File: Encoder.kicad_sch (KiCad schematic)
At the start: 13 parts, among them U5 AS5047D

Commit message: Add mcu connections
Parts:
- TP1, TP2, TP3, TP4, TP5, TP6: footprint (none) -> TestPoint:TestPoint_Pad_D1.0mm
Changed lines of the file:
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@@
 			)
 		)
-		(property "Footprint" ""
+		(property "Footprint" "TestPoint:TestPoint_Pad_D1.0mm"
 			(at 186.69 93.98 0)
 			(effects
@@
 			)
 		)
-		(property "Footprint" ""
+		(property "Footprint" "TestPoint:TestPoint_Pad_D1.0mm"
 			(at 173.99 85.09 0)
 			(effects
@@
 			)
 		)
-		(property "Footprint" ""
+		(property "Footprint" "TestPoint:TestPoint_Pad_D1.0mm"
 			(at 158.75 85.09 0)
 			(effects
@@
 			)
 		)
-		(property "Footprint" ""
+		(property "Footprint" "TestPoint:TestPoint_Pad_D1.0mm"
 			(at 166.37 85.09 0)
 			(effects
@@
 			)
 		)
-		(property "Footprint" ""
+		(property "Footprint" "TestPoint:TestPoint_Pad_D1.0mm"
 			(at 179.07 93.98 0)
 			(effects
@@
 			)
 		)
-		(property "Footprint" ""
+		(property "Footprint" "TestPoint:TestPoint_Pad_D1.0mm"
 			(at 194.31 93.98 0)
 			(effects

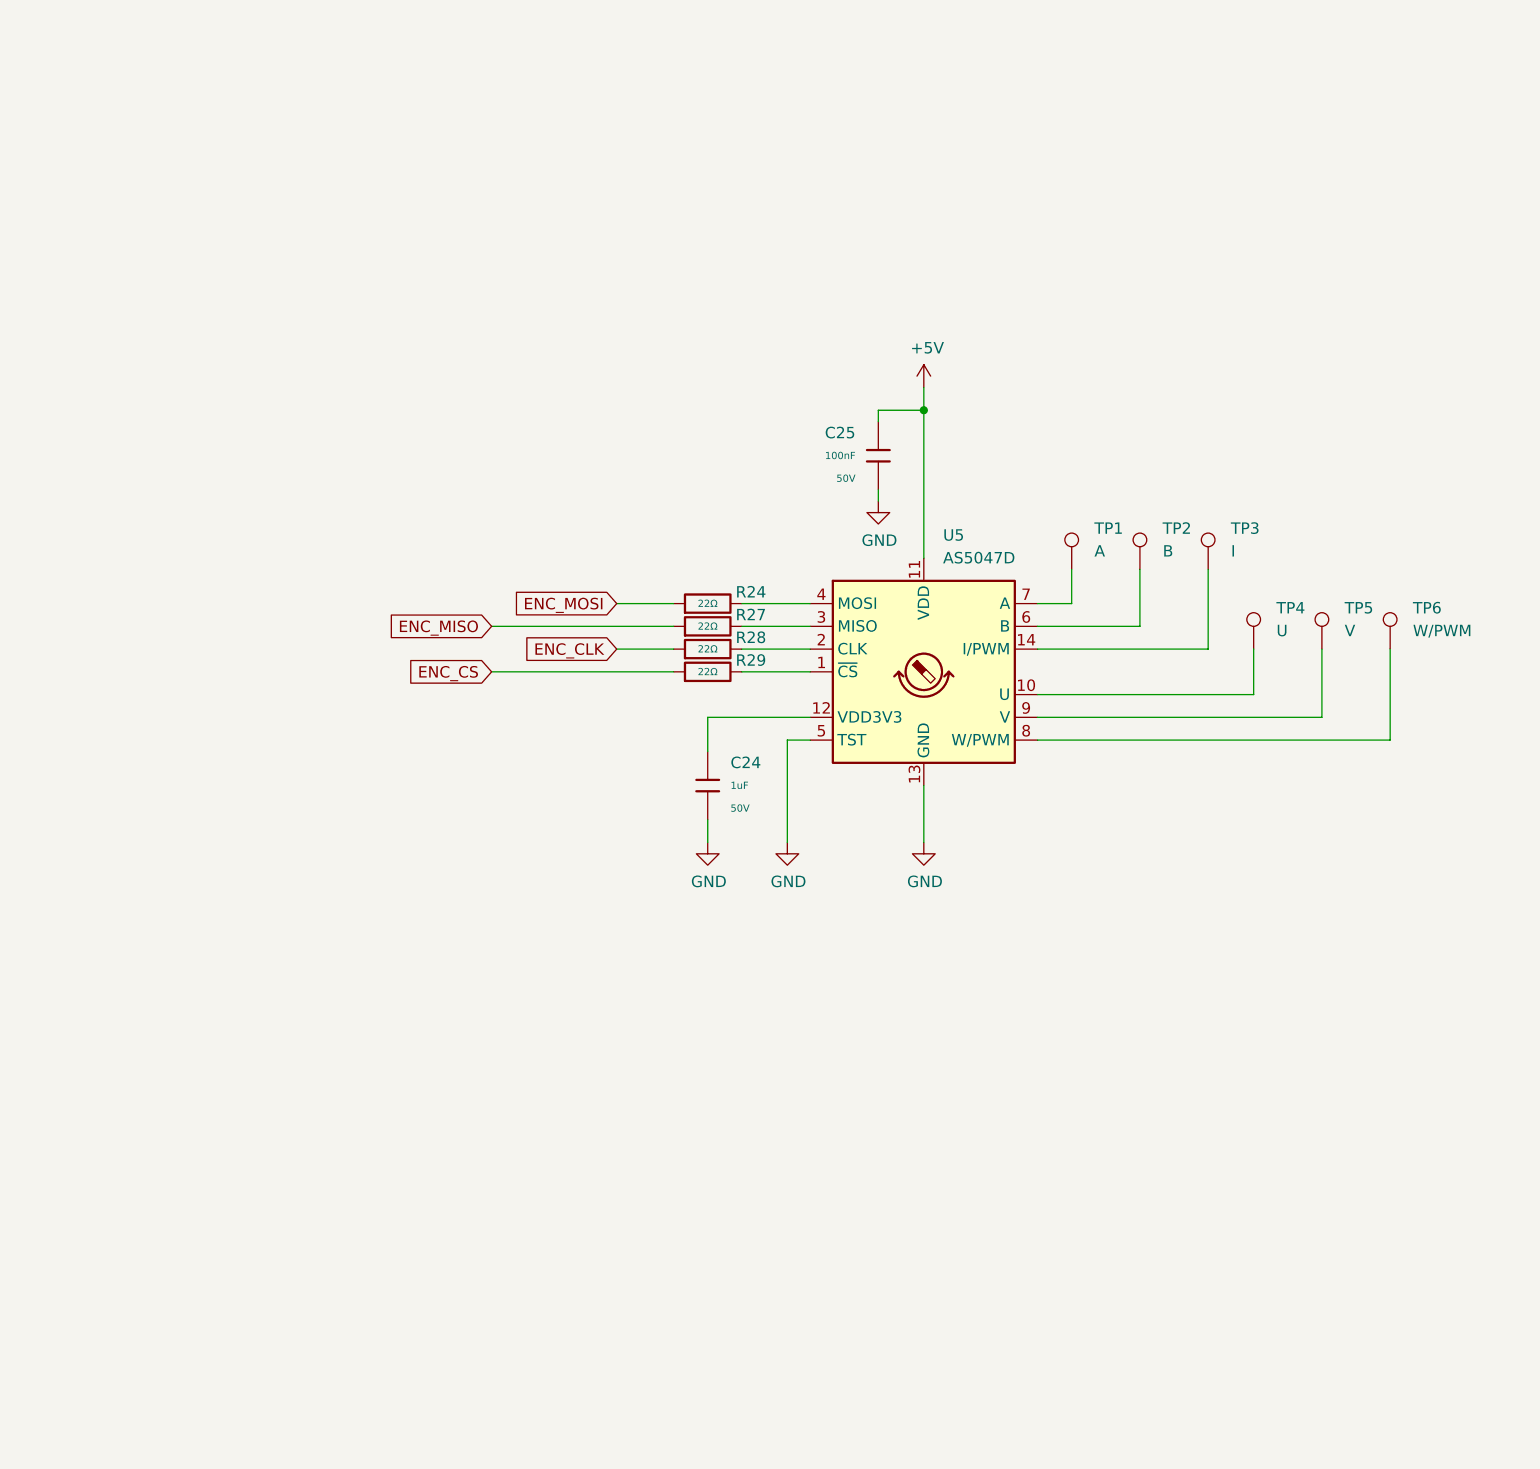
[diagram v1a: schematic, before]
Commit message: Added DRV layout
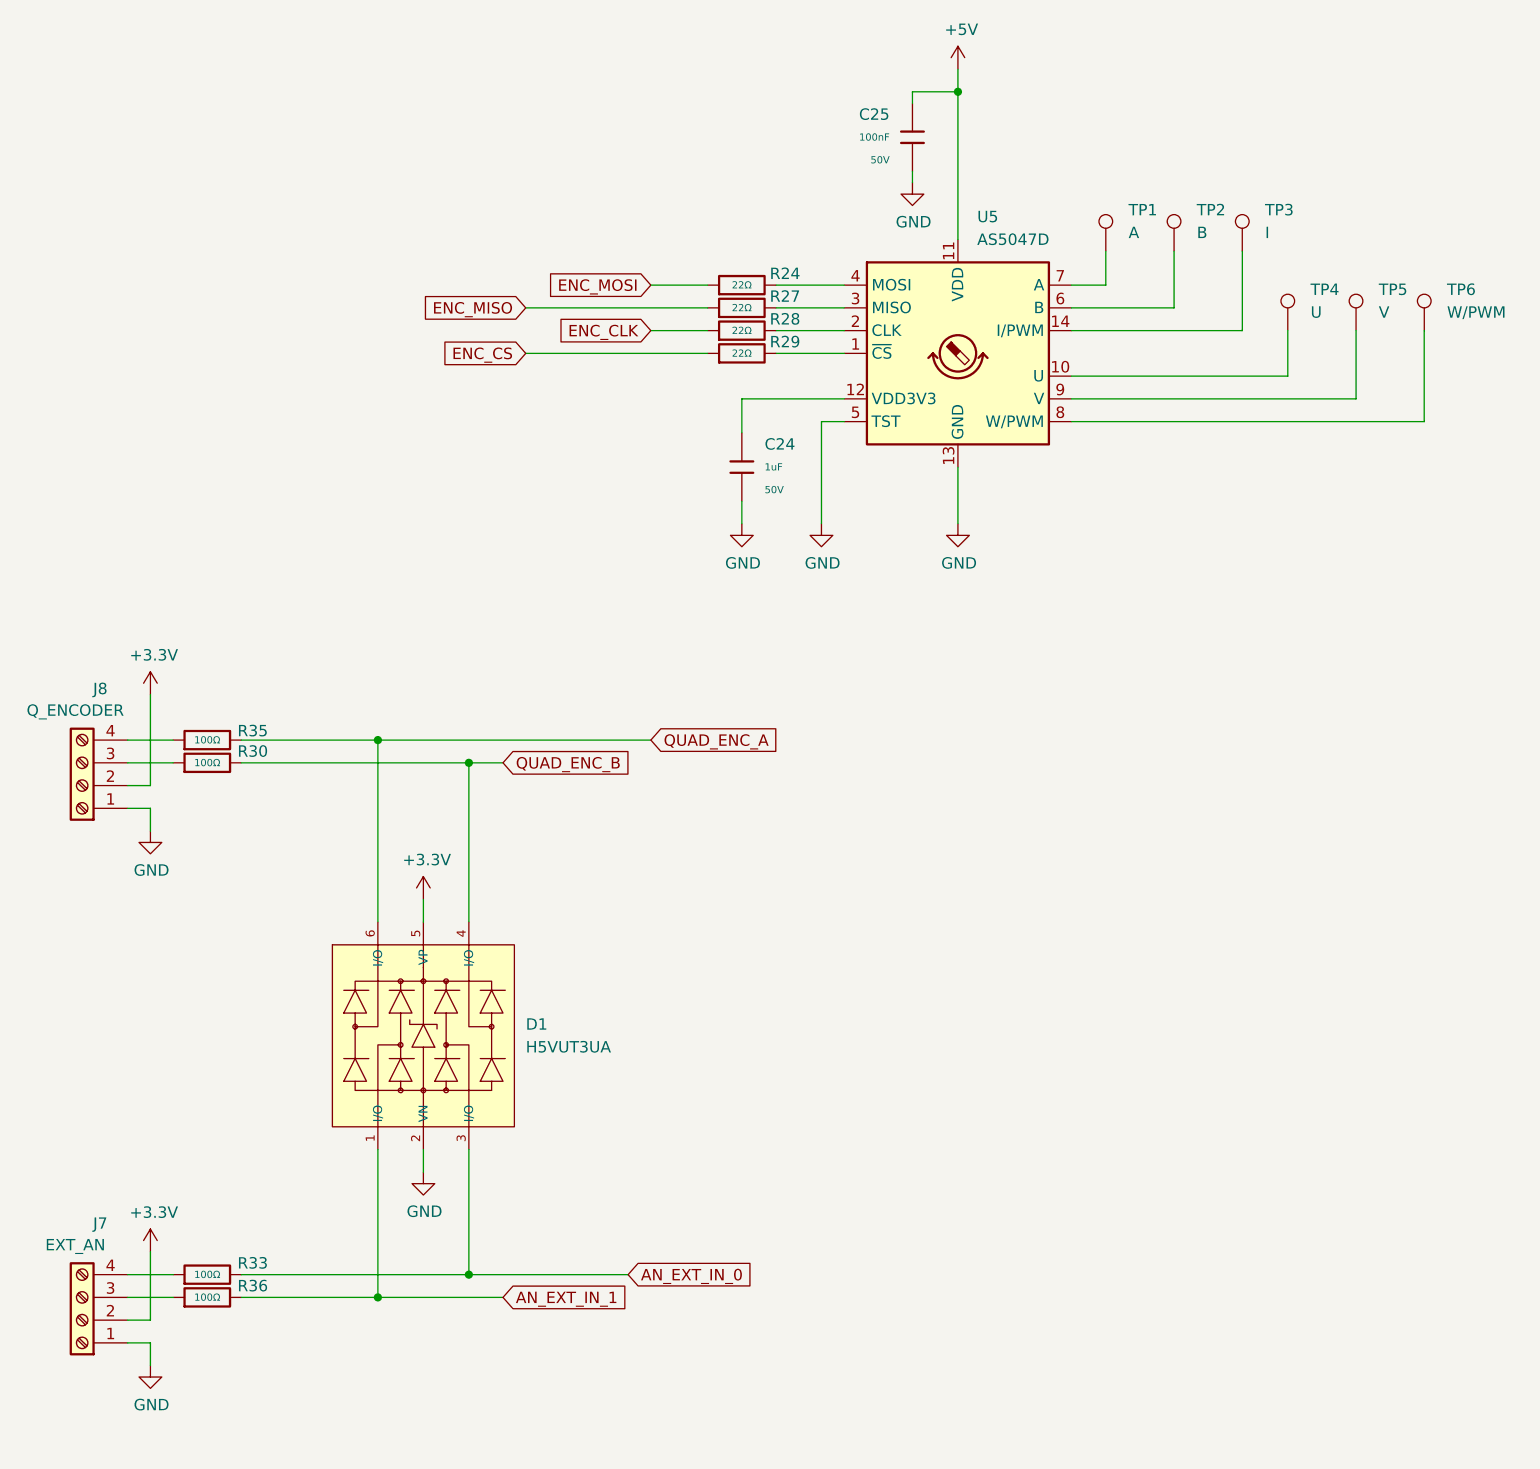
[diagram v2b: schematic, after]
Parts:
- added D1: H5VUT3UA, PCM_JLCPCB:SOT-363_L2.1-W1.3-P0.65-LS2.2-BL, symbol PCM_JLCPCB-Diode-Packages:Package, H5VUT3UA
- added J7: EXT_AN, Connector_JST:JST_XH_B4B-XH-A_1x04_P2.50mm_Vertical, symbol Connector:Screw_Terminal_01x04
- added J8: Q_ENCODER, Connector_JST:JST_XH_B4B-XH-A_1x04_P2.50mm_Vertical, symbol Connector:Screw_Terminal_01x04
- added R30, R33, R35, R36: 100Ω, PCM_JLCPCB:R_0603, symbol PCM_JLCPCB-Resistors:0603,100Ω
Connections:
- net GND: now also D1.2 (VN), J7.1 (Pin_1), J8.1 (Pin_1)
- new net: J8.3 (Pin_3), R30.1
- new net: J8.4 (Pin_4), R35.1
- new net: J7.3 (Pin_3), R36.1
- new net: J7.4 (Pin_4), R33.1
- new net +3.3V: D1.5 (VP), J7.2 (Pin_2), J8.2 (Pin_2)
- new net AN_EXT_IN_0: D1.3 (I/O), R33.2
- new net AN_EXT_IN_1: D1.1 (I/O), R36.2
- new net QUAD_ENC_A: D1.6 (I/O), R35.2
- new net QUAD_ENC_B: D1.4 (I/O), R30.2
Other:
- moved on the sheet: C24, C25, R24, R27, R28, R29, TP1, TP2, TP3, TP4, TP5, TP6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

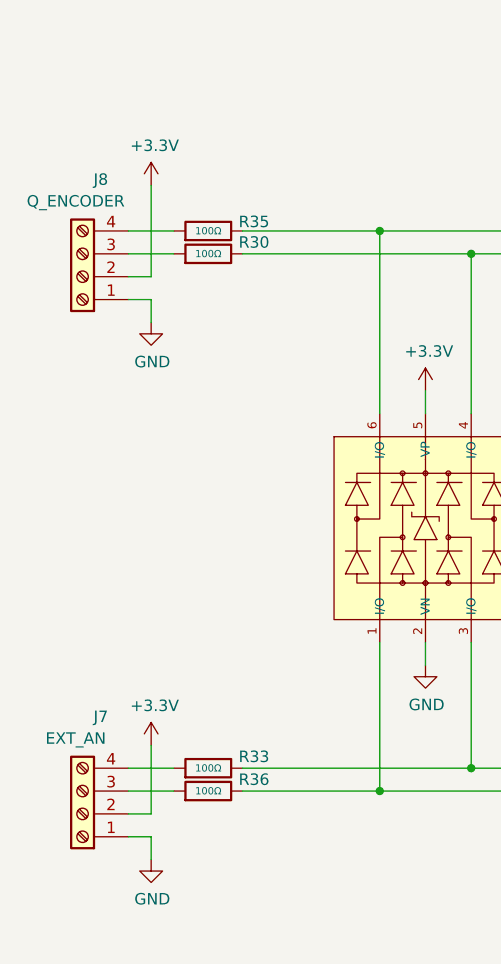
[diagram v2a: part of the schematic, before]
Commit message: updated mcu connections
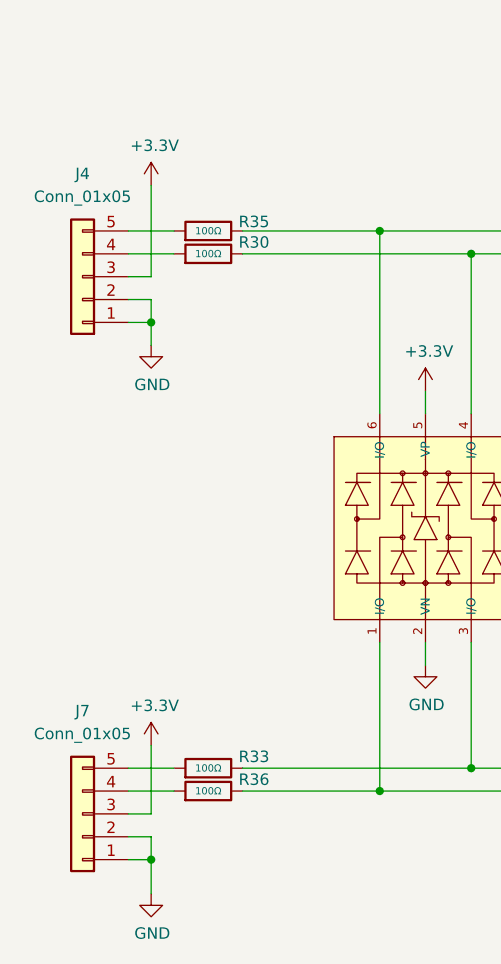
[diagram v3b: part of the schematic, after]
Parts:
- removed J7: EXT_AN, Connector_JST:JST_XH_B4B-XH-A_1x04_P2.50mm_Vertical, symbol Connector:Screw_Terminal_01x04
- removed J8: Q_ENCODER, Connector_JST:JST_XH_B4B-XH-A_1x04_P2.50mm_Vertical, symbol Connector:Screw_Terminal_01x04
- added J4, J7: Conn_01x05, Connector_JST:JST_GH_SM04B-GHS-TB_1x04-1MP_P1.25mm_Horizontal, symbol Connector_Generic:Conn_01x05
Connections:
- net +3.3V: now also J4.3 (Pin_3), J7.3 (Pin_3)
- net GND: now also J4.1 (Pin_1), J4.2 (Pin_2), J7.1 (Pin_1), J7.2 (Pin_2)
- net at R30.1: now also J4.4 (Pin_4)
- net at R35.1: now also J4.5 (Pin_5)
- net at R36.1: now also J7.4 (Pin_4)
- net at R33.1: now also J7.5 (Pin_5)
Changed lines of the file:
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@@
 	)
 	(junction
+		(at 50.8 114.3)
+		(diameter 0)
+		(color 0 0 0 0)
+	)
+	(junction
 		(at 76.2 104.14)
 		(diameter 0)
@@
 		(color 0 0 0 0)
 	)
+	(junction
+		(at 50.8 173.99)
+		(diameter 0)
+		(color 0 0 0 0)
+	)
 	(wire
 		(pts
@@
 	(wire
 		(pts
-			(xy 50.8 173.99) (xy 50.8 171.45)
+			(xy 50.8 177.8) (xy 50.8 173.99)
 		)
 		(stroke
@@
 	(wire
 		(pts
-			(xy 50.8 114.3) (xy 50.8 111.76)
+			(xy 50.8 116.84) (xy 50.8 114.3)
 		)
 		(stroke
@@
 	(wire
 		(pts
+			(xy 48.26 114.3) (xy 50.8 114.3)
+		)
+		(stroke
+			(width 0)
+			(type default)
+		)
+	)
+	(wire
+		(pts
 			(xy 86.36 106.68) (xy 86.36 124.46)
 		)
@@
 	(wire
 		(pts
+			(xy 48.26 173.99) (xy 50.8 173.99)
+		)
+		(stroke
+			(width 0)
+			(type default)
+		)
+	)
+	(wire
+		(pts
 			(xy 165.1 55.88) (xy 165.1 49.53)
 		)
@@
 	(wire
 		(pts
+			(xy 50.8 114.3) (xy 50.8 111.76)
+		)
+		(stroke
+			(width 0)
+			(type default)
+		)
+	)
+	(wire
+		(pts
 			(xy 50.8 109.22) (xy 48.26 109.22)
 		)
@@
 	(wire
 		(pts
+			(xy 50.8 173.99) (xy 50.8 171.45)
+		)
+		(stroke
+			(width 0)
+			(type default)
+		)
+	)
+	(wire
+		(pts
 			(xy 135.89 31.75) (xy 140.97 31.75)
 		)
@@
 	)
 	(symbol
-		(lib_id "Connector:Screw_Terminal_01x04")
-		(at 43.18 109.22 180)
-		(unit 1)
-		(exclude_from_sim no)
-		(in_bom yes)
-		(on_board yes)
-		(dnp no)
-		(property "Reference" "J8"
-			(at 45.212 98.425 0)
-			(effects
-				(font
-					(size 1.27 1.27)
-				)
-			)
-		)
-		(property "Value" "Q_ENCODER"
-			(at 42.418 100.838 0)
-			(effects
-				(font
-					(size 1.27 1.27)
-				)
-			)
-		)
-		(property "Footprint" "Connector_JST:JST_XH_B4B-XH-A_1x04_P2.50mm_Vertical"
-			(at 43.18 109.22 0)
-			(effects
-				(font
-					(size 1.27 1.27)
-				)
-				(hide yes)
-			)
-		)
-		(property "Datasheet" "~"
-			(at 43.18 109.22 0)
-			(effects
-				(font
-					(size 1.27 1.27)
-				)
-				(hide yes)
-			)
-		)
-		(property "Description" ""
-			(at 43.18 109.22 0)
-			(effects
-				(font
-					(size 1.27 1.27)
-				)
-			)
-		)
-		(pin "1"
-		)
-		(pin "2"
-		)
-		(pin "3"
-		)
-		(pin "4"
-		)
-		(instances
-			(project "PiccoloMotorDriver"
-				(path "/cc8a13e7-b1a6-4cbd-adcd-4feb8b2e2369/b5037c4c-8129-4a92-a0a6-b41a7050a316"
-					(reference "J8")
-					(unit 1)
-				)
-			)
-		)
-	)
-	(symbol
 		(lib_id "power:+3.3V")
 		(at 50.8 161.29 0)
@@
 	(symbol
 		(lib_id "power:GND")
-		(at 50.8 173.99 0)
+		(at 50.8 177.8 0)
 		(unit 1)
 		(exclude_from_sim no)
@@
 		(dnp no)
 		(property "Reference" "#PWR056"
-			(at 50.8 180.34 0)
+			(at 50.8 184.15 0)
 			(effects
 				(font
@@
 		)
 		(property "Value" "GND"
-			(at 50.927 178.3842 0)
+			(at 50.927 182.1942 0)
 			(effects
 				(font
@@
 		)
 		(property "Footprint" ""
-			(at 50.8 173.99 0)
+			(at 50.8 177.8 0)
 			(effects
 				(font
@@
 		)
 		(property "Datasheet" ""
-			(at 50.8 173.99 0)
+			(at 50.8 177.8 0)
 			(effects
 				(font
@@
 		)
 		(property "Description" ""
-			(at 50.8 173.99 0)
+			(at 50.8 177.8 0)
 			(effects
 				(font
@@
 	(symbol
 		(lib_id "power:GND")
-		(at 50.8 114.3 0)
+		(at 50.8 116.84 0)
 		(unit 1)
 		(exclude_from_sim no)
@@
 		(dnp no)
 		(property "Reference" "#PWR054"
-			(at 50.8 120.65 0)
+			(at 50.8 123.19 0)
 			(effects
 				(font
@@
 		)
 		(property "Value" "GND"
-			(at 50.927 118.6942 0)
+			(at 50.927 121.2342 0)
 			(effects
 				(font
@@
 		)
 		(property "Footprint" ""
-			(at 50.8 114.3 0)
+			(at 50.8 116.84 0)
 			(effects
 				(font
@@
 		)
 		(property "Datasheet" ""
-			(at 50.8 114.3 0)
+			(at 50.8 116.84 0)
 			(effects
 				(font
@@
 		)
 		(property "Description" ""
-			(at 50.8 114.3 0)
+			(at 50.8 116.84 0)
 			(effects
 				(font
@@
 	)
 	(symbol
+		(lib_id "Connector_Generic:Conn_01x05")
+		(at 43.18 168.91 180)
+		(unit 1)
+		(exclude_from_sim no)
+		(in_bom yes)
+		(on_board yes)
+		(dnp no)
+		(fields_autoplaced yes)
+		(property "Reference" "J7"
+			(at 43.18 157.48 0)
+			(effects
+				(font
+					(size 1.27 1.27)
+				)
+			)
+		)
+		(property "Value" "Conn_01x05"
+			(at 43.18 160.02 0)
+			(effects
+				(font
+					(size 1.27 1.27)
+				)
+			)
+		)
+		(property "Footprint" "Connector_JST:JST_GH_SM04B-GHS-TB_1x04-1MP_P1.25mm_Horizontal"
+			(at 43.18 168.91 0)
+			(effects
+				(font
+					(size 1.27 1.27)
+				)
+				(hide yes)
+			)
+		)
+		(property "Datasheet" "~"
+			(at 43.18 168.91 0)
+			(effects
+				(font
+					(size 1.27 1.27)
+				)
+				(hide yes)
+			)
+		)
+		(property "Description" "Generic connector, single row, 01x05, script generated (kicad-library-utils/schlib/autogen/connector/)"
+			(at 43.18 168.91 0)
+			(effects
+				(font
+					(size 1.27 1.27)
+				)
+				(hide yes)
+			)
+		)
+		(pin "1"
+		)
+		(pin "2"
+		)
+		(pin "4"
+		)
+		(pin "5"
+		)
+		(pin "3"
+		)
+		(instances
+			(project "PiccoloMotorDriver"
+				(path "/cc8a13e7-b1a6-4cbd-adcd-4feb8b2e2369/b5037c4c-8129-4a92-a0a6-b41a7050a316"
+					(reference "J7")
+					(unit 1)
+				)
+			)
+		)
+	)
+	(symbol
 		(lib_id "power:+5V")
 		(at 140.97 29.21 0)
@@
 	)
 	(symbol
+		(lib_id "Connector_Generic:Conn_01x05")
+		(at 43.18 109.22 180)
+		(unit 1)
+		(exclude_from_sim no)
+		(in_bom yes)
+		(on_board yes)
+		(dnp no)
+		(fields_autoplaced yes)
+		(property "Reference" "J4"
+			(at 43.18 97.79 0)
+			(effects
+				(font
+					(size 1.27 1.27)
+				)
+			)
+		)
+		(property "Value" "Conn_01x05"
+			(at 43.18 100.33 0)
+			(effects
+				(font
+					(size 1.27 1.27)
+				)
+			)
+		)
+		(property "Footprint" "Connector_JST:JST_GH_SM04B-GHS-TB_1x04-1MP_P1.25mm_Horizontal"
+			(at 43.18 109.22 0)
+			(effects
+				(font
+					(size 1.27 1.27)
+				)
+				(hide yes)
+			)
+		)
+		(property "Datasheet" "~"
+			(at 43.18 109.22 0)
+			(effects
+				(font
+					(size 1.27 1.27)
+				)
+				(hide yes)
+			)
+		)
+		(property "Description" "Generic connector, single row, 01x05, script generated (kicad-library-utils/schlib/autogen/connector/)"
+			(at 43.18 109.22 0)
+			(effects
+				(font
+					(size 1.27 1.27)
+				)
+				(hide yes)
+			)
+		)
+		(pin "1"
+		)
+		(pin "2"
+		)
+		(pin "4"
+		)
+		(pin "5"
+		)
+		(pin "3"
+		)
+		(instances
+			(project ""
+				(path "/cc8a13e7-b1a6-4cbd-adcd-4feb8b2e2369/b5037c4c-8129-4a92-a0a6-b41a7050a316"
+					(reference "J4")
+					(unit 1)
+				)
+			)
+		)
+	)
+	(symbol
 		(lib_id "PCM_JLCPCB-Resistors:0603,22Ω")
 		(at 116.84 58.42 90)
@@
 					(unit 1)
 				)
-			)
-		)
-	)
-	(symbol
-		(lib_id "Connector:Screw_Terminal_01x04")
-		(at 43.18 168.91 180)
-		(unit 1)
-		(exclude_from_sim no)
-		(in_bom yes)
-		(on_board yes)
-		(dnp no)
-		(property "Reference" "J7"
-			(at 45.212 158.115 0)
-			(effects
-				(font
-					(size 1.27 1.27)
-				)
-			)
-		)
-		(property "Value" "EXT_AN"
-			(at 42.418 160.528 0)
-			(effects
-				(font
-					(size 1.27 1.27)
-				)
-			)
-		)
-		(property "Footprint" "Connector_JST:JST_XH_B4B-XH-A_1x04_P2.50mm_Vertical"
-			(at 43.18 168.91 0)
-			(effects
-				(font
-					(size 1.27 1.27)
-				)
-				(hide yes)
-			)
-		)
-		(property "Datasheet" "~"
-			(at 43.18 168.91 0)
-			(effects
-				(font
-					(size 1.27 1.27)
-				)
-				(hide yes)
-			)
-		)
-		(property "Description" ""
-			(at 43.18 168.91 0)
-			(effects
-				(font
-					(size 1.27 1.27)
-				)
-			)
-		)
-		(pin "1"
-		)
-		(pin "2"
-		)
-		(pin "3"
-		)
-		(pin "4"
-		)
-		(instances
-			(project "PiccoloMotorDriver"
-				(path "/cc8a13e7-b1a6-4cbd-adcd-4feb8b2e2369/b5037c4c-8129-4a92-a0a6-b41a7050a316"
-					(reference "J7")
-					(unit 1)
-				)

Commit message: layout placement
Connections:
- net GND: now also J4.4 (Pin_4), J4.5 (Pin_5), J7.4 (Pin_4), J7.5 (Pin_5); no longer J4.1 (Pin_1), J4.2 (Pin_2), J7.1 (Pin_1), J7.2 (Pin_2)
- net at R36.1: now also J7.2 (Pin_2); no longer J7.4 (Pin_4)
- net at R35.1: now also J4.1 (Pin_1); no longer J4.5 (Pin_5)
- net at R33.1: now also J7.1 (Pin_1); no longer J7.5 (Pin_5)
- net at R30.1: now also J4.2 (Pin_2); no longer J4.4 (Pin_4)
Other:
- moved on the sheet: J4, J7
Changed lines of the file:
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@@
 	(symbol
 		(lib_id "Connector_Generic:Conn_01x05")
-		(at 43.18 168.91 180)
+		(at 43.18 168.91 0)
+		(mirror y)
 		(unit 1)
 		(exclude_from_sim no)
@@
 		(on_board yes)
 		(dnp no)
-		(fields_autoplaced yes)
 		(property "Reference" "J7"
-			(at 43.18 157.48 0)
+			(at 43.18 180.34 0)
 			(effects
 				(font
@@
 		)
 		(property "Value" "Conn_01x05"
-			(at 43.18 160.02 0)
+			(at 43.18 177.8 0)
 			(effects
 				(font
@@
 	(symbol
 		(lib_id "Connector_Generic:Conn_01x05")
-		(at 43.18 109.22 180)
+		(at 43.18 109.22 0)
+		(mirror y)
 		(unit 1)
 		(exclude_from_sim no)
@@
 		(on_board yes)
 		(dnp no)
-		(fields_autoplaced yes)
 		(property "Reference" "J4"
-			(at 43.18 97.79 0)
+			(at 43.18 120.65 0)
 			(effects
 				(font
@@
 		)
 		(property "Value" "Conn_01x05"
-			(at 43.18 100.33 0)
-			(effects
-				(font
+			(at 43.18 118.11 0)
+			(effects
+				(font
